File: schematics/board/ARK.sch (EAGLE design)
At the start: 215 parts, among them IC1 STM32F103C8T, Q5 8MHz

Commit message: Незначительные изменения в платах БСК1 и АРК
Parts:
- R100, R80, R84, R85, R86: value 1k2 -> 2k
- renumbered U$58 to INA219#1
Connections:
- net BUSPLUS: now also LED4.C
- net VDD: no longer LED4.C
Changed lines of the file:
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@@
 <part name="R56" library="rcl" library_urn="urn:adsk.eagle:library:334" deviceset="R-US_" device="R2512" package3d_urn="urn:adsk.eagle:package:23545/2" value="R05"/>
 <part name="U$57" library="CanCubeSat" deviceset="INA219AID" device=""/>
-<part name="U$58" library="CanCubeSat" deviceset="INA219AID" device=""/>
+<part name="INA219#1" library="CanCubeSat" deviceset="INA219AID" device=""/>
 <part name="U$59" library="CanCubeSat" deviceset="LTC3119" device=""/>
 <part name="C33" library="rcl" library_urn="urn:adsk.eagle:library:334" deviceset="C-US" device="C0603" package3d_urn="urn:adsk.eagle:package:23616/2" value="0,1µ"/>
@@
 <part name="R79" library="resistor" library_urn="urn:adsk.eagle:library:348" deviceset="R-US_" device="R0603" package3d_urn="urn:adsk.eagle:package:23555/3" value="10k"/>
 <part name="LED3" library="led" library_urn="urn:adsk.eagle:library:259" deviceset="LED" device="CHIPLED_0603" package3d_urn="urn:adsk.eagle:package:15822/2"/>
-<part name="R80" library="resistor" library_urn="urn:adsk.eagle:library:348" deviceset="R-US_" device="R0603" package3d_urn="urn:adsk.eagle:package:23555/3" value="1k2"/>
+<part name="R80" library="resistor" library_urn="urn:adsk.eagle:library:348" deviceset="R-US_" device="R0603" package3d_urn="urn:adsk.eagle:package:23555/3" value="2k"/>
 <part name="LED4" library="led" library_urn="urn:adsk.eagle:library:259" deviceset="LED" device="CHIPLED_0603" package3d_urn="urn:adsk.eagle:package:15822/2"/>
 <part name="R83" library="resistor" library_urn="urn:adsk.eagle:library:348" deviceset="R-US_" device="R0603" package3d_urn="urn:adsk.eagle:package:23555/3" value="2k"/>
 <part name="LED5" library="led" library_urn="urn:adsk.eagle:library:259" deviceset="LED" device="CHIPLED_0603" package3d_urn="urn:adsk.eagle:package:15822/2"/>
-<part name="R84" library="resistor" library_urn="urn:adsk.eagle:library:348" deviceset="R-US_" device="R0603" package3d_urn="urn:adsk.eagle:package:23555/3" value="1k2"/>
+<part name="R84" library="resistor" library_urn="urn:adsk.eagle:library:348" deviceset="R-US_" device="R0603" package3d_urn="urn:adsk.eagle:package:23555/3" value="2k"/>
 <part name="LED6" library="led" library_urn="urn:adsk.eagle:library:259" deviceset="LED" device="CHIPLED_0603" package3d_urn="urn:adsk.eagle:package:15822/2"/>
-<part name="R85" library="resistor" library_urn="urn:adsk.eagle:library:348" deviceset="R-US_" device="R0603" package3d_urn="urn:adsk.eagle:package:23555/3" value="1k2"/>
+<part name="R85" library="resistor" library_urn="urn:adsk.eagle:library:348" deviceset="R-US_" device="R0603" package3d_urn="urn:adsk.eagle:package:23555/3" value="2k"/>
 <part name="LED7" library="led" library_urn="urn:adsk.eagle:library:259" deviceset="LED" device="CHIPLED_0603" package3d_urn="urn:adsk.eagle:package:15822/2"/>
-<part name="R86" library="resistor" library_urn="urn:adsk.eagle:library:348" deviceset="R-US_" device="R0603" package3d_urn="urn:adsk.eagle:package:23555/3" value="1k2"/>
+<part name="R86" library="resistor" library_urn="urn:adsk.eagle:library:348" deviceset="R-US_" device="R0603" package3d_urn="urn:adsk.eagle:package:23555/3" value="2k"/>
 <part name="LED8" library="led" library_urn="urn:adsk.eagle:library:259" deviceset="LED" device="CHIPLED_0603" package3d_urn="urn:adsk.eagle:package:15822/2"/>
-<part name="R100" library="resistor" library_urn="urn:adsk.eagle:library:348" deviceset="R-US_" device="R0603" package3d_urn="urn:adsk.eagle:package:23555/3" value="1k2"/>
+<part name="R100" library="resistor" library_urn="urn:adsk.eagle:library:348" deviceset="R-US_" device="R0603" package3d_urn="urn:adsk.eagle:package:23555/3" value="2k"/>
 <part name="C32" library="rcl" library_urn="urn:adsk.eagle:library:334" deviceset="C-US" device="C0603" package3d_urn="urn:adsk.eagle:package:23616/2" value="0,1µ"/>
 <part name="C43" library="rcl" library_urn="urn:adsk.eagle:library:334" deviceset="C-US" device="C1206" package3d_urn="urn:adsk.eagle:package:23618/2" value="10µ"/>
@@
 </instance>
 <instance part="U$57" gate="G$1" x="543.56" y="238.76" smashed="yes" rot="R270"/>
-<instance part="U$58" gate="G$1" x="563.88" y="238.76" smashed="yes" rot="R270"/>
+<instance part="INA219#1" gate="G$1" x="563.88" y="238.76" smashed="yes" rot="R270"/>
 <instance part="U$59" gate="G$1" x="500.38" y="142.24" smashed="yes"/>
 <instance part="C33" gate="G$1" x="522.986" y="153.67" smashed="yes" rot="R270">
@@
 <wire x1="562.61" y1="91.44" x2="562.61" y2="213.868" width="0.1524" layer="91"/>
 <junction x="548.64" y="91.44"/>
-<pinref part="U$58" gate="G$1" pin="GND"/>
+<pinref part="INA219#1" gate="G$1" pin="GND"/>
 <wire x1="562.61" y1="213.868" x2="562.61" y2="226.06" width="0.1524" layer="91"/>
 <pinref part="U$57" gate="G$1" pin="GND"/>
@@
 </segment>
 <segment>
-<pinref part="U$58" gate="G$1" pin="A0"/>
-<pinref part="U$58" gate="G$1" pin="A1"/>
+<pinref part="INA219#1" gate="G$1" pin="A0"/>
+<pinref part="INA219#1" gate="G$1" pin="A1"/>
 <wire x1="565.15" y1="251.46" x2="567.69" y2="251.46" width="0.1524" layer="91"/>
 <wire x1="567.69" y1="251.46" x2="567.69" y2="260.858" width="0.1524" layer="91"/>
@@
 <wire x1="577.85" y1="173.482" x2="567.69" y2="173.482" width="0.1524" layer="91"/>
 <junction x="577.85" y="167.386"/>
-<pinref part="U$58" gate="G$1" pin="IN+"/>
+<pinref part="INA219#1" gate="G$1" pin="IN+"/>
 <wire x1="567.69" y1="173.482" x2="567.69" y2="226.06" width="0.1524" layer="91"/>
 </segment>
@@
 <pinref part="R74" gate="G$1" pin="2"/>
 <wire x1="565.15" y1="161.798" x2="565.15" y2="167.386" width="0.1524" layer="91"/>
-<pinref part="U$58" gate="G$1" pin="IN-"/>
+<pinref part="INA219#1" gate="G$1" pin="IN-"/>
 <wire x1="565.15" y1="167.386" x2="565.15" y2="226.06" width="0.1524" layer="91"/>
 <junction x="565.15" y="167.386"/>
@@
 <pinref part="U$57" gate="G$1" pin="SCL"/>
 <wire x1="539.75" y1="251.46" x2="539.75" y2="261.62" width="0.1524" layer="91"/>
-<pinref part="U$58" gate="G$1" pin="SCL"/>
+<pinref part="INA219#1" gate="G$1" pin="SCL"/>
 <wire x1="560.07" y1="251.46" x2="560.07" y2="261.62" width="0.1524" layer="91"/>
 <wire x1="560.07" y1="261.62" x2="539.75" y2="261.62" width="0.1524" layer="91"/>
@@
 <pinref part="U$57" gate="G$1" pin="SDA"/>
 <wire x1="542.29" y1="251.46" x2="542.29" y2="256.54" width="0.1524" layer="91"/>
-<pinref part="U$58" gate="G$1" pin="SDA"/>
+<pinref part="INA219#1" gate="G$1" pin="SDA"/>
 <wire x1="562.61" y1="251.46" x2="562.61" y2="256.54" width="0.1524" layer="91"/>
 <wire x1="562.61" y1="256.54" x2="542.29" y2="256.54" width="0.1524" layer="91"/>
@@
 <segment>
 <wire x1="535.94" y1="254" x2="535.94" y2="223.52" width="0.1524" layer="91"/>
-<pinref part="U$58" gate="G$1" pin="VCC"/>
+<pinref part="INA219#1" gate="G$1" pin="VCC"/>
 <wire x1="535.94" y1="223.52" x2="539.75" y2="223.52" width="0.1524" layer="91"/>
 <wire x1="539.75" y1="223.52" x2="560.07" y2="223.52" width="0.1524" layer="91"/>
@@
 </segment>
 <segment>
-<pinref part="LED4" gate="G$1" pin="C"/>
-<wire x1="109.22" y1="292.1" x2="96.52" y2="292.1" width="0.1524" layer="91"/>
-<label x="96.52" y="292.1" size="1.778" layer="95"/>
-</segment>
-<segment>
 <pinref part="U$16" gate="G$1" pin="SVCC"/>
 <wire x1="731.52" y1="140.97" x2="726.44" y2="140.97" width="0.1524" layer="91"/>
@@
 </segment>
 <segment>
+<pinref part="LED4" gate="G$1" pin="C"/>
+<wire x1="109.22" y1="292.1" x2="96.52" y2="292.1" width="0.1524" layer="91"/>
+<label x="96.52" y="292.1" size="1.778" layer="95"/>
+</segment>
+<segment>

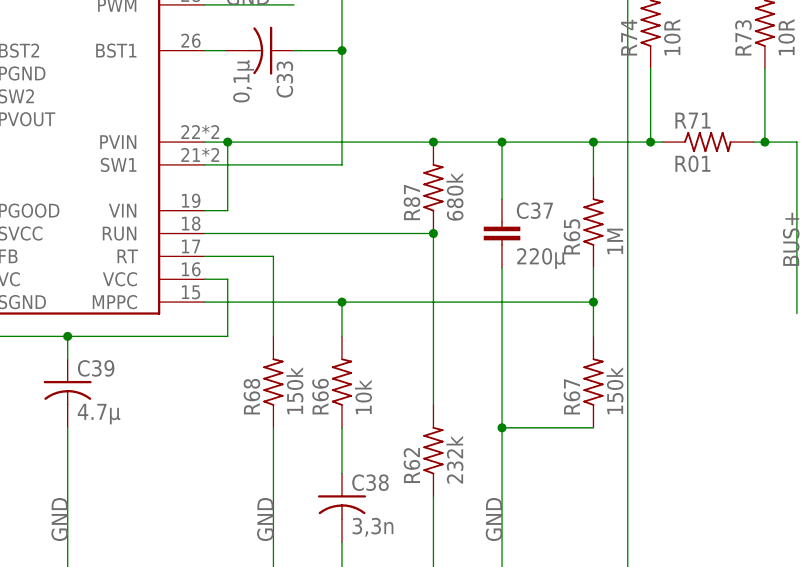
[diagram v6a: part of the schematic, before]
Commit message: В плате АРК разведены дорожки групп BMS и всех DC-DC. Остался МК и его обвес
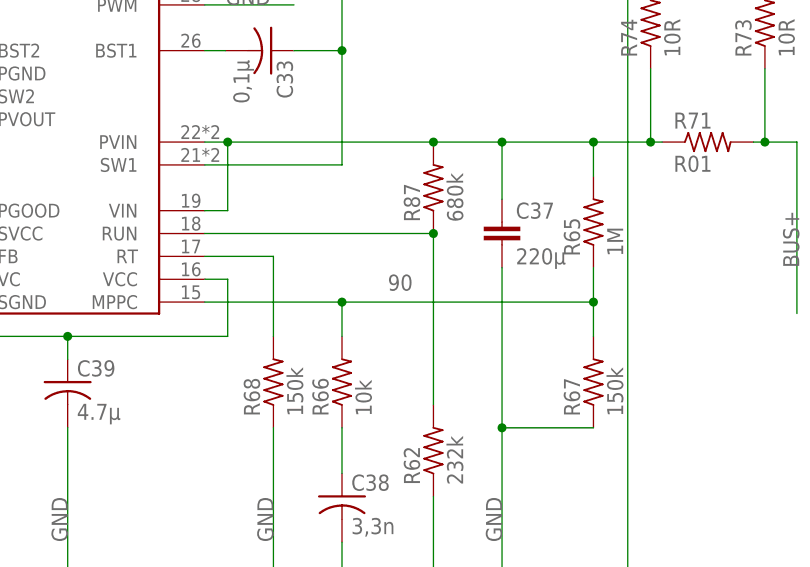
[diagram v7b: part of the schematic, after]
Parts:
- renumbered U$22 to AD5272#2
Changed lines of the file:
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@@
 <part name="C16" library="rcl" library_urn="urn:adsk.eagle:library:334" deviceset="C-US" device="C0603" package3d_urn="urn:adsk.eagle:package:23616/2" value="0,1µ"/>
 <part name="R61" library="resistor" library_urn="urn:adsk.eagle:library:348" deviceset="R-US_" device="R0603" package3d_urn="urn:adsk.eagle:package:23555/3" value="680k"/>
-<part name="U$22" library="CanCubeSat" deviceset="AD5272" device=""/>
+<part name="AD5272#2" library="CanCubeSat" deviceset="AD5272" device=""/>
 <part name="C29" library="rcl" library_urn="urn:adsk.eagle:library:334" deviceset="C-US" device="C0603" package3d_urn="urn:adsk.eagle:package:23616/2" value="1µ"/>
 <part name="C30" library="rcl" library_urn="urn:adsk.eagle:library:334" deviceset="C-US" device="C0603" package3d_urn="urn:adsk.eagle:package:23616/2" value="680p"/>
@@
 <attribute name="VALUE" x="694.182" y="143.002" size="1.778" layer="96" rot="R90"/>
 </instance>
-<instance part="U$22" gate="G$1" x="660.4" y="121.92" smashed="yes" rot="R180"/>
+<instance part="AD5272#2" gate="G$1" x="660.4" y="121.92" smashed="yes" rot="R180"/>
 <instance part="C29" gate="G$1" x="677.418" y="131.826" smashed="yes">
 <attribute name="NAME" x="678.434" y="132.461" size="1.778" layer="95"/>
@@
 </segment>
 <segment>
-<pinref part="U$22" gate="G$1" pin="VSS"/>
-<pinref part="U$22" gate="G$1" pin="W"/>
+<pinref part="AD5272#2" gate="G$1" pin="VSS"/>
+<pinref part="AD5272#2" gate="G$1" pin="W"/>
 <wire x1="673.1" y1="121.92" x2="683.26" y2="121.92" width="0.1524" layer="91"/>
 <wire x1="683.26" y1="121.92" x2="683.26" y2="124.46" width="0.1524" layer="91"/>
@@
 <wire x1="683.26" y1="137.16" x2="647.7" y2="137.16" width="0.1524" layer="91"/>
 <junction x="683.26" y="124.46"/>
-<pinref part="U$22" gate="G$1" pin="GND"/>
+<pinref part="AD5272#2" gate="G$1" pin="GND"/>
 <wire x1="647.7" y1="137.16" x2="647.7" y2="127" width="0.1524" layer="91"/>
 <wire x1="647.7" y1="137.16" x2="647.7" y2="146.05" width="0.1524" layer="91"/>
@@
 <wire x1="677.418" y1="126.746" x2="677.418" y2="124.46" width="0.1524" layer="91"/>
 <junction x="677.418" y="124.46"/>
-<pinref part="U$22" gate="G$1" pin="ADDR"/>
+<pinref part="AD5272#2" gate="G$1" pin="ADDR"/>
 <wire x1="647.7" y1="116.84" x2="627.38" y2="116.84" width="0.1524" layer="91"/>
 <wire x1="627.38" y1="116.84" x2="627.38" y2="137.16" width="0.1524" layer="91"/>
@@
 <wire x1="558.8" y1="121.92" x2="558.8" y2="125.73" width="0.1524" layer="91"/>
 <junction x="558.8" y="125.73"/>
+<label x="535.94" y="127" size="1.778" layer="95"/>
 </segment>
 </net>
@@
 </segment>
 <segment>
-<pinref part="U$22" gate="G$1" pin="SCL"/>
+<pinref part="AD5272#2" gate="G$1" pin="SCL"/>
 <wire x1="647.7" y1="119.38" x2="637.54" y2="119.38" width="0.1524" layer="91"/>
 <label x="640.08" y="119.38" size="1.778" layer="95"/>
@@
 </segment>
 <segment>
-<pinref part="U$22" gate="G$1" pin="SDA"/>
+<pinref part="AD5272#2" gate="G$1" pin="SDA"/>
 <wire x1="647.7" y1="121.92" x2="637.54" y2="121.92" width="0.1524" layer="91"/>
 <label x="640.08" y="121.92" size="1.778" layer="95"/>
@@
 <net name="N$51" class="0">
 <segment>
-<pinref part="U$22" gate="G$1" pin="CAP"/>
+<pinref part="AD5272#2" gate="G$1" pin="CAP"/>
 <wire x1="673.1" y1="127" x2="673.1" y2="134.62" width="0.1524" layer="91"/>
 <pinref part="C29" gate="G$1" pin="1"/>
@@
 <pinref part="R30" gate="G$1" pin="1"/>
 <wire x1="690.88" y1="124.46" x2="690.88" y2="119.38" width="0.1524" layer="91"/>
-<pinref part="U$22" gate="G$1" pin="A"/>
+<pinref part="AD5272#2" gate="G$1" pin="A"/>
 <wire x1="673.1" y1="119.38" x2="685.8" y2="119.38" width="0.1524" layer="91"/>
 <wire x1="685.8" y1="119.38" x2="690.88" y2="119.38" width="0.1524" layer="91"/>
@@
 <junction x="676.148" y="116.84"/>
 <pinref part="C52" gate="G$1" pin="1"/>
-<pinref part="U$22" gate="G$1" pin="VDD"/>
+<pinref part="AD5272#2" gate="G$1" pin="VDD"/>
 <wire x1="685.8" y1="119.38" x2="685.8" y2="116.84" width="0.1524" layer="91"/>
 <junction x="685.8" y="119.38"/>
@@
 <net name="DPD_RST" class="0">
 <segment>
-<pinref part="U$22" gate="G$1" pin="RESET"/>
+<pinref part="AD5272#2" gate="G$1" pin="RESET"/>
 <wire x1="647.7" y1="124.46" x2="635" y2="124.46" width="0.1524" layer="91"/>
 <label x="635" y="124.46" size="1.778" layer="95"/>

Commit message: В плате АРК разведено еще больше дорожек - до 99%. Надо заменить МК или подключить текущий МК к GND
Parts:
- added R101, R102: 4k7, resistor:R-US_R0603
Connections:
- new net N$26: C31.1, U$16.MPPC, U$16.SVCC, U$16.VCC
- net BMS+: now also LED3.C, LED4.C, LED5.C, LED6.C, LED7.C, LED8.C
- net BMS1: now also IC1MCU.PA5; no longer IC1MCU.PA1
- net BMS2: now also IC1MCU.PA6; no longer IC1MCU.PA2
- net BMS5: now also IC1MCU.PA1; no longer IC1MCU.PA5
- net BMS6: now also IC1MCU.PA2; no longer IC1MCU.PA6
- net BUSPLUS: no longer LED3.C, LED4.C, LED5.C, LED6.C, LED7.C, LED8.C
- net SCL: now also R101.2
- net SDA: now also R102.2
- net VDD: now also R101.1, R102.1; no longer C31.1, U$16.MPPC, U$16.SVCC, U$16.VCC
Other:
- moved on the sheet: LED2, R81
